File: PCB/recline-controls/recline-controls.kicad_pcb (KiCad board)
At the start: 2 copper layers, 109 x 84 mm, 79 parts, among them J1 DX07S016JA1R1500, J10 0705550036, J11 0705550036, J2 Conn_01x03, J3 RJHSE-5381, J4 1757242, J5 PPPC052LFBN-RC, J6 0705530002, J7 0705530002, J8 0705530002, J9 0705550036, M1 D24V22F5, M2 D24V22F3, SW1 TL3330AF260QG, SW2 TL3330AF260QG, U1 TEMPLATE, U2 RP2040, U3 MAX3535ECWI+T, X1 ABM8G-12.000MHZ-18-D2Y-T

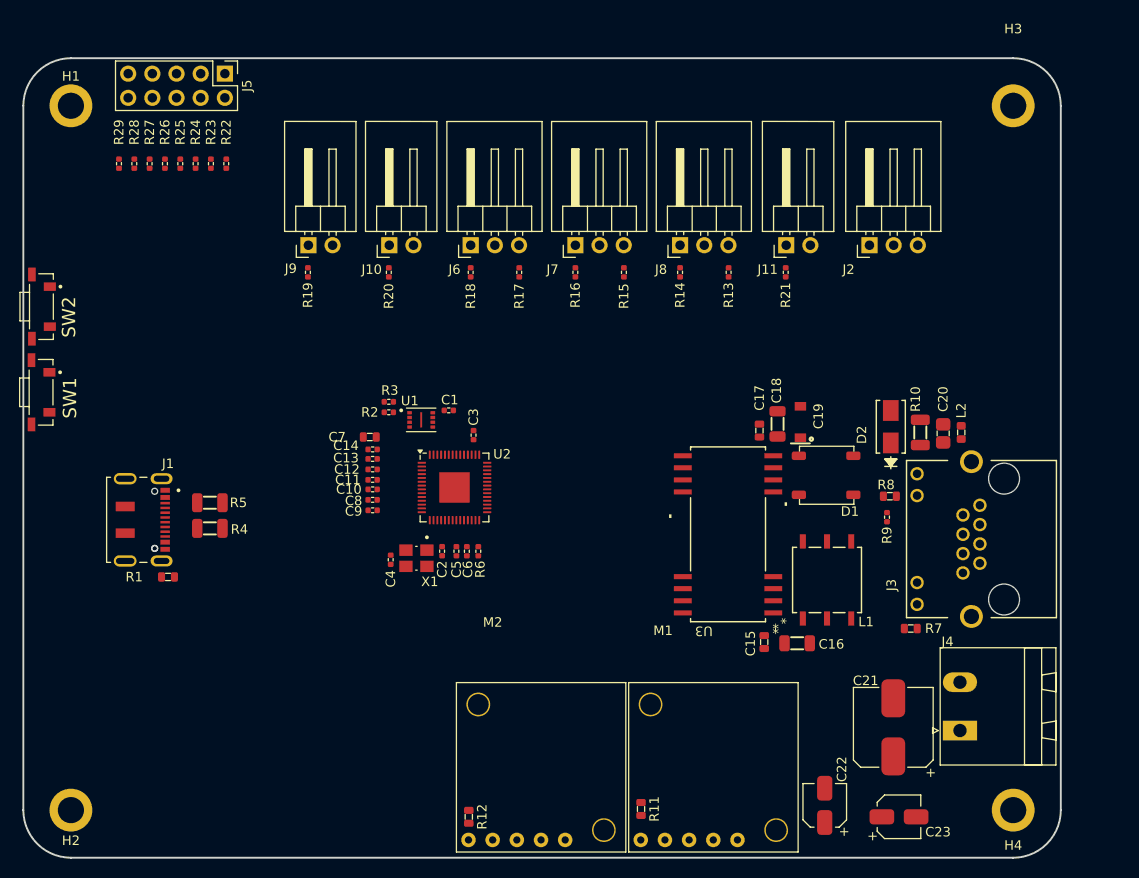
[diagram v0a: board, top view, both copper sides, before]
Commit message: All Hardware Tweaked / 3D Renders
PCBs for Actuator Control, Recline Control HID, and 7 Segment carrier are all complete with full 3D models rendering. 3D Renders of all board added to repository img directory.
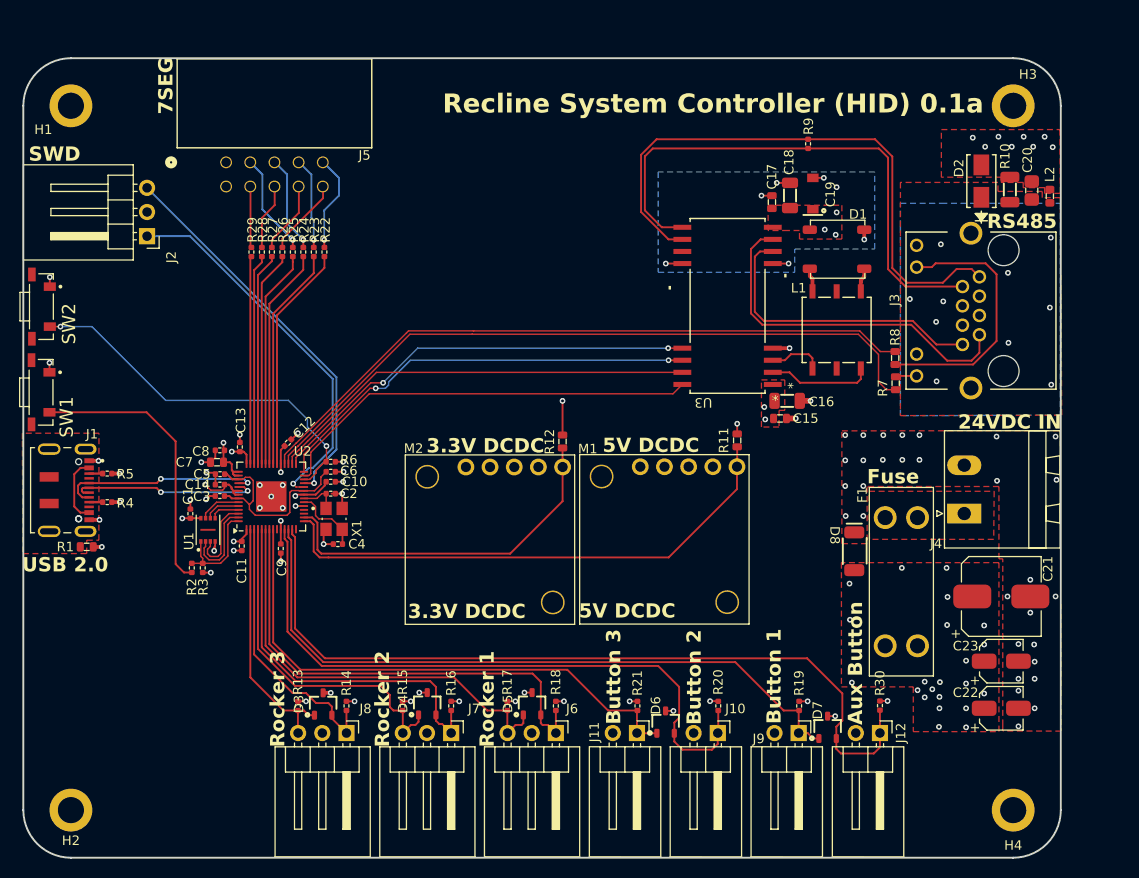
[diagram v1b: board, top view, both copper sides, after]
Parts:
- added D3: PESD3V3L2BT,215, AVR-KiCAD-Lib-Diodes:SOT-23, F.Cu at (131.5, 123.8)
- added D4: PESD3V3L2BT,215, AVR-KiCAD-Lib-Diodes:SOT-23, F.Cu at (142.4, 123.8)
- added D5: PESD3V3L2BT,215, AVR-KiCAD-Lib-Diodes:SOT-23, F.Cu at (153.4, 123.8)
- added D6: PESD3V3L2BT,215, AVR-KiCAD-Lib-Diodes:SOT-23, F.Cu at (167.5, 125.8)
- added D7: PESD3V3L2BT,215, AVR-KiCAD-Lib-Diodes:SOT-23, F.Cu at (184.5, 126.3)
- added D8: SMAJ24A, AVR-KiCAD-Lib-Diodes:SMAJ, F.Cu at (187.3, 107.8)
- added F1: 3557-2, AVR-KiCAD-Lib-Fuse-Holders:FUSE_3557-2, F.Cu at (192.2, 111.0)
- added J12: 0705550036, AVR-KiCAD-Lib-Connectors:Pin_Header_Angled_1x02_Pitch2.54mm, F.Cu at (190.0, 126.9)
- added R30: RC0402FR-071KL, AVR-KiCAD-Lib-Resistors:R0402, F.Cu at (190.0, 124.0)
- D2: value SMAJ30CA -> SMASeries
- J5: value PPPC052LFBN-RC -> SBH11-PBPC-D05-RA-BK; footprint AVR-KiCAD-Lib-Connectors:PPPC052LFBN-RC_2x05_Pitch2.54mm -> AVR-KiCAD-Lib-Connectors:CONN10_D05-RA-BK_SUL
- R4, R5: value RC1206FR-075K1L -> RC0402FR-075K1L; footprint AVR-KiCAD-Lib-Resistors:R1206 -> AVR-KiCAD-Lib-Resistors:R0402
- moved J2 75.9 mm to (113.0, 74.7), turned to 180 degrees
- moved J9 72.7 mm to (181.5, 126.9), turned to -90 degrees
- moved R19 68.8 mm to (181.5, 124.0), turned to 90 degrees
- moved R13 64.2 mm to (128.8, 124.0)
- moved J8 62.1 mm to (133.9, 126.9), turned to -90 degrees
- moved J10 61.8 mm to (173.0, 126.9), turned to -90 degrees
- moved R14 57.5 mm to (133.9, 124.0), turned to 90 degrees
- moved R20 57.2 mm to (173.0, 124.0), turned to 90 degrees
- moved J11 53.6 mm to (164.5, 126.9), turned to -90 degrees
- moved J7 52.9 mm to (144.9, 126.9), turned to -90 degrees
- moved J6 52.0 mm to (155.9, 126.9), turned to -90 degrees
- moved R15 51.1 mm to (139.8, 124.0), turned to 90 degrees
- moved R21 48.1 mm to (164.5, 124.0), turned to 90 degrees
- moved R16 47.4 mm to (144.9, 124.0), turned to 90 degrees
- moved R18 46.4 mm to (155.9, 124.0), turned to 90 degrees
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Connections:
- net Net-(J2-Pin_1) renamed /RP2040/SWCLK
- net Net-(J2-Pin_3) renamed /RP2040/SWD
- J4 pad 1: +24V -> Net-(F1-Pad2)
- J5 pad 1: Net-(J5-Pad1) -> GND
- J5 pad 10: GND -> Net-(J5-Pad10)
- J5 pad 2: Net-(J5-Pad2) -> GND
- J5 pad 9: GND -> Net-(J5-Pad9)
- R22 pad 2: Net-(J5-Pad1) -> Net-(J5-Pad9)
- R23 pad 2: Net-(J5-Pad3) -> Net-(J5-Pad7)
- R25 pad 2: Net-(J5-Pad7) -> Net-(J5-Pad3)
- R26 pad 2: Net-(J5-Pad2) -> Net-(J5-Pad10)
- R27 pad 2: Net-(J5-Pad4) -> Net-(J5-Pad8)
- R29 pad 2: Net-(J5-Pad8) -> Net-(J5-Pad4)
- U2 pad 11: unconnected-(U2-GPIO8-Pad11) -> /Controls and Switches/BUTTON2
- U2 pad 12: unconnected-(U2-GPIO9-Pad12) -> /Controls and Switches/BUTTON1
- U2 pad 13: unconnected-(U2-GPIO10-Pad13) -> /Controls and Switches/AUXBUTTON
- U2 pad 15: unconnected-(U2-GPIO12-Pad15) -> /Power/5V_PG
- U2 pad 16: unconnected-(U2-GPIO13-Pad16) -> /Power/3.3V_PG
- U2 pad 2: unconnected-(U2-GPIO0-Pad2) -> /Controls and Switches/ROCKER3_B
- U2 pad 27: unconnected-(U2-GPIO16-Pad27) -> /RP2040/RS485_TXD
- U2 pad 28: unconnected-(U2-GPIO17-Pad28) -> /RP2040/RS485_RXD
- U2 pad 29: unconnected-(U2-GPIO18-Pad29) -> /RP2040/RS485_TX_EN
- U2 pad 3: unconnected-(U2-GPIO1-Pad3) -> /Controls and Switches/ROCKER3_A
- U2 pad 30: unconnected-(U2-GPIO19-Pad30) -> /RP2040/RS485_RX_EN
- U2 pad 31: unconnected-(U2-GPIO20-Pad31) -> /RP2040/RS485_RX_LED
- U2 pad 32: unconnected-(U2-GPIO21-Pad32) -> /RP2040/RS485_TX_LED
- U2 pad 34: unconnected-(U2-GPIO22-Pad34) -> /7 Segment Display/7SEG0
- U2 pad 35: unconnected-(U2-GPIO23-Pad35) -> /7 Segment Display/7SEG1
- U2 pad 36: unconnected-(U2-GPIO24-Pad36) -> /7 Segment Display/7SEG2
- U2 pad 37: unconnected-(U2-GPIO25-Pad37) -> /7 Segment Display/7SEG3
- U2 pad 38: unconnected-(U2-GPIO26_ADC0-Pad38) -> /7 Segment Display/7SEG4
- U2 pad 39: unconnected-(U2-GPIO27_ADC1-Pad39) -> /7 Segment Display/7SEG5
- U2 pad 4: unconnected-(U2-GPIO2-Pad4) -> /Controls and Switches/ROCKER2_B
- U2 pad 40: unconnected-(U2-GPIO28_ADC2-Pad40) -> /7 Segment Display/7SEG6
- U2 pad 41: unconnected-(U2-GPIO29_ADC3-Pad41) -> /7 Segment Display/7SEG7
- U2 pad 5: unconnected-(U2-GPIO3-Pad5) -> /Controls and Switches/ROCKER2_A
- U2 pad 6: unconnected-(U2-GPIO4-Pad6) -> /Controls and Switches/ROCKER1_B
- U2 pad 7: unconnected-(U2-GPIO5-Pad7) -> /Controls and Switches/ROCKER1_A
- U2 pad 8: unconnected-(U2-GPIO6-Pad8) -> /Controls and Switches/BUTTON3
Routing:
- net /Controls and Switches/AUXBUTTON: track 0.00 -> 85.9 mm
- net /RP2040/RS485_RX_LED: track 0.00 -> 74.0 mm
- net /Controls and Switches/BUTTON1: track 0.00 -> 72.3 mm
- net /RP2040/RS485_TX_LED: track 0.00 -> 71.4 mm
- net /Controls and Switches/BUTTON2: track 0.00 -> 69.1 mm
- net /RS485 Transceiver/A_RS485: track 0.00 -> 61.8 mm
- net /Controls and Switches/BUTTON3: track 0.00 -> 57.6 mm
- net /RS485 Transceiver/B_RS485: track 0.00 -> 56.9 mm
- net /Power/5V_PG: track 0.00 -> 56.1 mm
- net /Controls and Switches/ROCKER1_A: track 0.00 -> 51.0 mm
- net /RP2040/RS485_TX_EN: track 0.00 -> 46.0 mm, vias 0 -> 2
- net /RP2040/RS485_RXD: track 0.00 -> 45.9 mm, vias 0 -> 2
- net /Controls and Switches/ROCKER1_B: track 0.00 -> 45.8 mm
- net /RP2040/RS485_RX_EN: track 0.00 -> 45.4 mm
- net /RP2040/RS485_TXD: track 0.00 -> 45.0 mm
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- added copper zone on F.Cu, net +24V
- added copper zone on In2.Cu, net +24V
- added copper zone on F.Cu, net +3.3V
- added copper zone on In2.Cu, net +3.3V
- added copper zone on F.Cu, net +5V
- added copper zone on In2.Cu, net +5V
- added copper zone on B.Cu, net /RS485 Transceiver/RJ45_SHIELD
- added copper zone on F.Cu, net /RS485 Transceiver/RJ45_SHIELD
- added copper zone on B.Cu, net Earth
- added copper zone on F.Cu, net GND
- added copper zone on In1.Cu, net GND
- added copper zone on In2.Cu, net GND
- added copper zone on F.Cu, net Net-(F1-Pad2)
- added copper zone on In2.Cu, net Net-(F1-Pad2)
- added copper zone on F.Cu, net Net-(J1-SHIELD-PadS1)
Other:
- copper layers 2 -> 4
- board text added: "24V"
- board text added: "24V Rail"
- board text added: "24VDC IN"
- board text added: "3.3V DCDC"
- board text added: "3V3 PG"
- board text added: "3V3 Rail"
- board text added: "5V DCDC"
- board text added: "5V PG"
- board text added: "5V Rail"
- board text added: "7SEG"
- board text added: "Accessibilita Project"
- board text added: "Aux Button"
- board text added: "Button 1"
- board text added: "Button 2"
- board text added: "Button 3"
- board text added: "Designed by Adam Vadala-Roth"
- board text added: "Fuse"
- board text added: "GND"
- board text added: "GPIO0"
- board text added: "GPIO1"
- board text added: "GPIO2"
- board text added: "GPIO3"
- board text added: "GPIO4"
- board text added: "GPIO5"
- board text added: "GPIO6"
- board text added: "GPIO8"
- board text added: "GPIO9"
- board text added: "GhostPCB LLC"
- board text added: "Mobility Independence Foundation"
- board text added: "RS485"
- board text added: "Recline System Controller (HID) 0.1a"
- board text added: "Reline Controller (Relcine-HID) 0.1a 2024"
- board text added: "Rocker 1"
- board text added: "Rocker 2"
- board text added: "Rocker 3"
- board text added: "SWCLK"
- board text added: "SWD"
- board text added: "USB 2.0"
- board text added: "https://github.com/Accessibilita"

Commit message: HID
Changes made to recline control HID board. Power input section redesigned, 5V regulator removed, RS485 circuit updated with fixes that other boards received. Redesign or internal plane topology following changes to RS485 section. Via stitching all around.
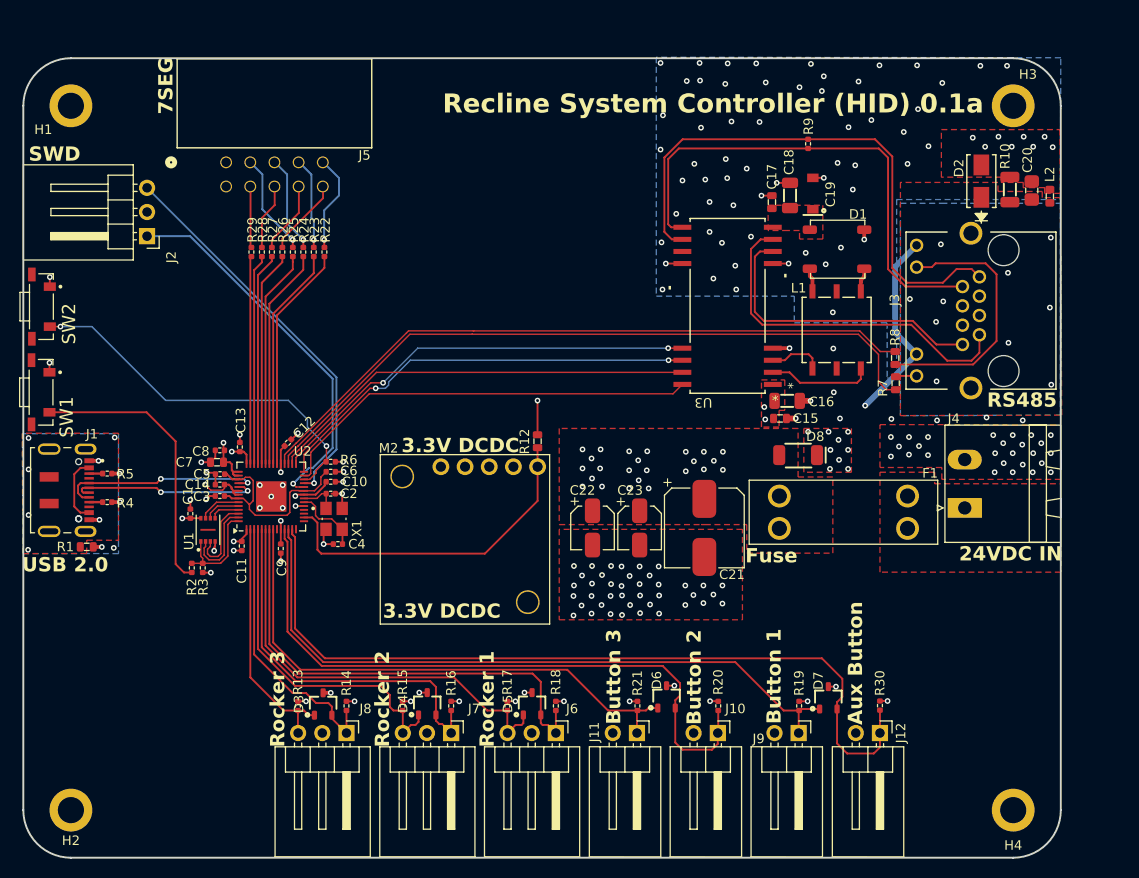
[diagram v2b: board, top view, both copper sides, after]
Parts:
- removed M1: D24V22F5, AVR-KiCAD-Lib-Modules:D24V22F12
- removed R11: RC0603FR-072K2L, AVR-KiCAD-Lib-Resistors:R0603
- D2: value SMASeries -> SMAJ30CA
- moved C22 46.9 mm to (159.8, 105.3), turned to -90 degrees
- moved C23 40.5 mm to (164.8, 105.3), turned to -90 degrees
- moved C21 32.0 mm to (171.6, 105.3), turned to -90 degrees
- moved D8 11.7 mm to (181.4, 97.7), turned to 180 degrees
- moved F1 9.50 mm to (186.2, 103.7), turned to 0 degrees
- moved D7 3.10 mm to (184.6, 123.2)
- moved D6 2.65 mm to (167.6, 123.1)
- moved M2 2.63 mm to (154.0, 98.9)
- moved R12 2.63 mm to (154.0, 96.2)
- moved J4 0.59 mm to (198.9, 103.2)
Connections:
- C20 pad 2: GND -> Earth
- D2 pad 2: GND -> Earth
- J3 pad 3: unconnected-(J3-Pad3) -> Earth
- J3 pad 4: unconnected-(J3-Pad4) -> Earth
- J3 pad 5: unconnected-(J3-Pad5) -> Earth
- J3 pad 6: unconnected-(J3-Pad6) -> Earth
- L2 pad 2: GND -> Earth
- R10 pad 1: GND -> Earth
- U2 pad 15: /Power/5V_PG -> unconnected-(U2-GPIO12-Pad15)
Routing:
- net /Power/5V_PG: track 56.1 -> 0.00 mm
- net GND: track 33.6 -> 54.5 mm, vias 72 -> 110
- net /RS485 Transceiver/B_RS485: track 56.9 -> 52.7 mm
- net /RS485 Transceiver/A_RS485: track 61.8 -> 58.0 mm
- net /Power/3.3V_PG: track 38.3 -> 35.7 mm
- net +3.3V: track 41.8 -> 40.7 mm, vias 24 -> 23
- net Net-(J1-SHIELD-PadS1): vias 0 -> 6
- net Earth: vias 6 -> 74
- net +5V: vias 4 -> 0
- net +24V: vias 22 -> 24
- added copper zone on F.Cu, net Earth
- added copper zone on In1.Cu, net Earth
- added copper zone on In2.Cu, net Earth
- added copper zone on B.Cu, net Net-(J1-SHIELD-PadS1)
- removed copper zone on In2.Cu, net +5V
- removed copper zone on In2.Cu, net GND
- removed copper zone on In2.Cu, net Net-(F1-Pad2)
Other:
- board text removed: "5V DCDC"
- board text removed: "5V PG"
- board text removed: "5V Rail"
